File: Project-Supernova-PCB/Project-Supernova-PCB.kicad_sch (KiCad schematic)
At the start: 0 parts

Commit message: Add more parts of schematic
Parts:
- added C1, C2: 10u, Capacitor_SMD:C_1206_3216Metric_Pad1.33x1.80mm_HandSolder, symbol Device:C_Polarized
- added C103: 4.7u, Capacitor_SMD:C_1206_3216Metric_Pad1.33x1.80mm_HandSolder, symbol Device:C
- added C104, C105: NC, Capacitor_SMD:C_1206_3216Metric_Pad1.33x1.80mm_HandSolder, symbol Device:C
- added C106: 100n, Capacitor_SMD:C_1206_3216Metric_Pad1.33x1.80mm_HandSolder, symbol Device:C
- added J103, J106, J109: Screw_Terminal_01x02, TerminalBlock:TerminalBlock_bornier-2_P5.08mm, symbol Connector:Screw_Terminal_01x02
- added J104, J105: Conn_01x02, Connector_PinHeader_2.54mm:PinHeader_1x02_P2.54mm_Vertical, symbol Connector_Generic:Conn_01x02
- added J107: Conn_Coaxial, symbol Connector:Conn_Coaxial
- added J108: Conn_01x04, Connector_PinHeader_2.54mm:PinHeader_1x04_P2.54mm_Vertical, symbol Connector_Generic:Conn_01x04
- added J6, J7: 100k_Thermistor, Connector_PinHeader_2.54mm:PinHeader_1x02_P2.54mm_Vertical, symbol Connector_Generic:Conn_01x02
- added L101: 0, Inductor_SMD:L_1206_3216Metric_Pad1.42x1.75mm_HandSolder, symbol Device:L
- added Q101: Si1470DH, Package_TO_SOT_SMD:SOT-363_SC-70-6, symbol Transistor_FET:Si1442DH
- added R103: 10k, Resistor_SMD:R_1206_3216Metric_Pad1.30x1.75mm_HandSolder, symbol Device:R
- added R104, R2, R3: 4.7k, Resistor_SMD:R_1206_3216Metric_Pad1.30x1.75mm_HandSolder, symbol Device:R
- added SW101: SW_SPST, symbol Switch:SW_SPST
- added U101: BMP280-Module, Project-Supernova-Footprint-Lib:BMP280-Module, symbol Project-Supernova-Symbol-Lib:BMP280-Module
- added U102: GY-NEO6MV2-Module, Project-Supernova-Footprint-Lib:GY-NEO6MV2-Module, symbol Project-Supernova-Symbol-Lib:GY-NEO6MV2-Module
- added U103: LoRa-E5, Project-Supernova-Footprint-Lib:LoRa-E5, symbol Project-Supernova-Symbol-Lib:LoRa-E5
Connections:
- new net: C104.1, L101.1, U103.15 (RFIO)
- new net: J109.1 (Pin_1), Q101.1 (D), Q101.2 (D), Q101.5 (D), Q101.6 (D)
- new net: C105.1, J107.1 (In), L101.2
- new net: J103.2 (Pin_2), J104.2 (Pin_2), SW101.1 (A)
- new net +3V3: C103.1, C106.1, J105.2 (Pin_2), J106.2 (Pin_2), J108.1 (Pin_1), U101.1 (VCC), U102.1 (VCC), U103.1 (VCC)
- new net +BATT: J109.2 (Pin_2), R103.1, SW101.2 (B)
- new net BATT_SENSE: R103.2, R104.1
- new net DHT_DATA: J108.2 (Pin_2)
- new net GND: C1.2, C103.2, C104.2, C105.2, C106.2, C2.2, J103.1 (Pin_1), J104.1 (Pin_1), J105.1 (Pin_1), J106.1 (Pin_1), J107.2 (Ext), J108.4 (Pin_4), J6.1 (Pin_1), J7.1 (Pin_1), Q101.4 (S), R104.2, U101.2 (GND), U102.4 (GND), U103.14 (GND), U103.16 (GND), U103.2 (GND), U103.22 (GND)
- new net HEATER_EN: Q101.3 (G)
- new net LORA_UART_MISO: U103.10 (PB6)
- new net LORA_UART_MOSI: U103.9 (PB7)
- new net TEMP_SENSE_1: C1.1, J6.2 (Pin_2), R2.2
- new net TEMP_SENSE_2: C2.1, J7.2 (Pin_2), R3.2
- new net TEMP_V+: R2.1, R3.1
- no-connect marks 0 -> 3
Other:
- note added: "Board Heater"
- note added: "Divider Ratio: 4.7k/14.7k = 0.3197x 10V battery turns into 3.2V max"
- note added: "Looking at screen part, with pins pointing down, Pin 1 is on the left"
- note added: "Power Switch"
- note added: "Radio Section"
- note added: "TODO LM335"
- note added: "TODO add IMU, maybe"
- note added: "TODO add a "flight mode" switch which indicates when it's launched for debugging"
- note added: "TODO add microcontroller"
- note added: "To DHT22"
- note added: "To Heater"

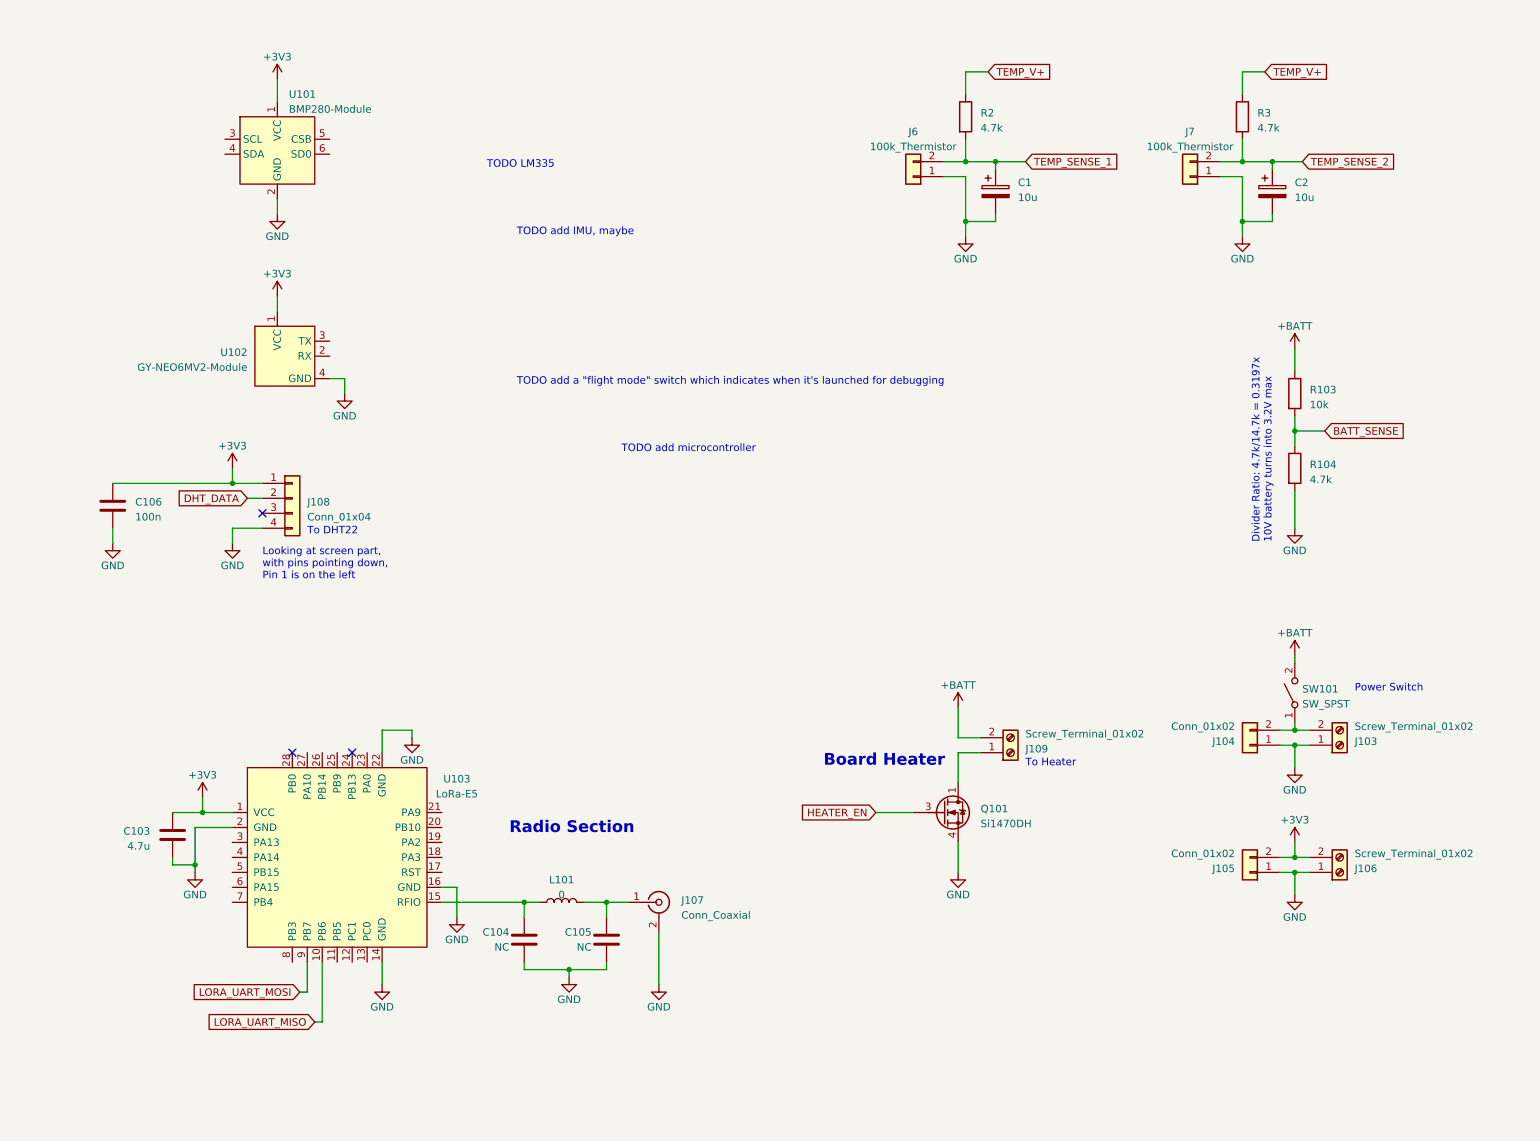
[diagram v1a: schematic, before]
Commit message: Update schematic docs, add TODO
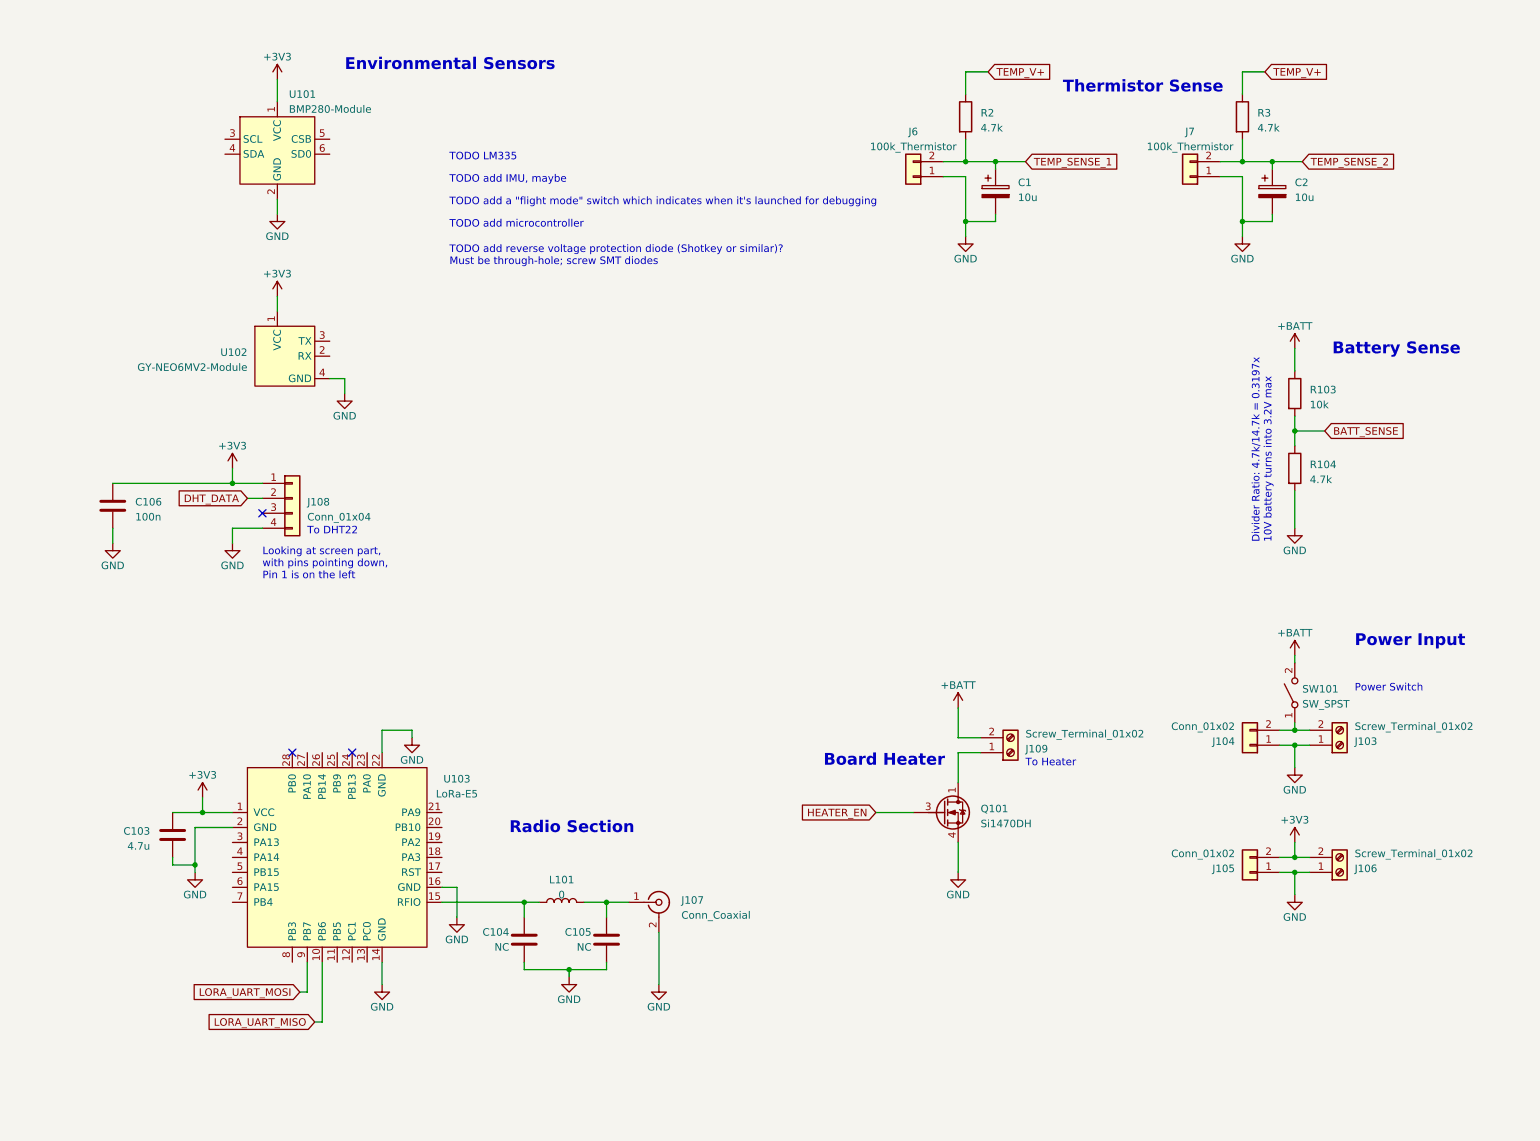
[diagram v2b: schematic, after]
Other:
- note added: "Battery Sense"
- note added: "Environmental Sensors"
- note added: "Power Input"
- note added: "TODO add reverse voltage protection diode (Shotkey or similar)? Must be through-hole; screw SMT diodes"
- note added: "Thermistor Sense"
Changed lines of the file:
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@@
   )
   (text "TODO add a \"flight mode\" switch which indicates when it's launched for debugging"
-    (at 99.06 77.47 0)
+    (at 87.63 46.99 0)
     (effects (font (size 1.27 1.27)) (justify left bottom))
   )
-  (text "TODO add microcontroller" (at 116.84 88.9 0)
+  (text "TODO add microcontroller" (at 87.63 50.8 0)
     (effects (font (size 1.27 1.27)) (justify left bottom))
   )
@@
     (at 55.88 110.49 0)
     (effects (font (size 1.27 1.27)) (justify left bottom))
+  )
+  (text "Power Input" (at 241.3 121.92 0)
+    (effects (font (size 2 2) (thickness 0.4) bold) (justify left bottom))
+  )
+  (text "TODO add reverse voltage protection diode (Shotkey or similar)?\nMust be through-hole; screw SMT diodes"
+    (at 87.63 57.15 0)
+    (effects (font (size 1.27 1.27)) (justify left bottom))
+  )
+  (text "Environmental Sensors" (at 69.85 24.13 0)
+    (effects (font (size 2 2) (thickness 0.4) bold) (justify left bottom))
   )
   (text "To Heater" (at 185.42 142.24 0)
@@
     (effects (font (size 1.27 1.27)) (justify left bottom))
   )
-  (text "TODO add IMU, maybe" (at 99.06 52.07 0)
+  (text "Thermistor Sense" (at 191.77 27.94 0)
+    (effects (font (size 2 2) (thickness 0.4) bold) (justify left bottom))
+  )
+  (text "TODO add IMU, maybe" (at 87.63 43.18 0)
     (effects (font (size 1.27 1.27)) (justify left bottom))
   )
-  (text "TODO LM335" (at 93.98 40.64 0)
+  (text "TODO LM335" (at 87.63 39.37 0)
     (effects (font (size 1.27 1.27)) (justify left bottom))
   )
+  (text "Battery Sense" (at 237.49 72.39 0)
+    (effects (font (size 2 2) (thickness 0.4) bold) (justify left bottom))
+  )
   (global_label "TEMP_V+" (shape input) (at 226.06 24.13 0) (fields_autoplaced)

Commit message: Add ESP32 microcontroller
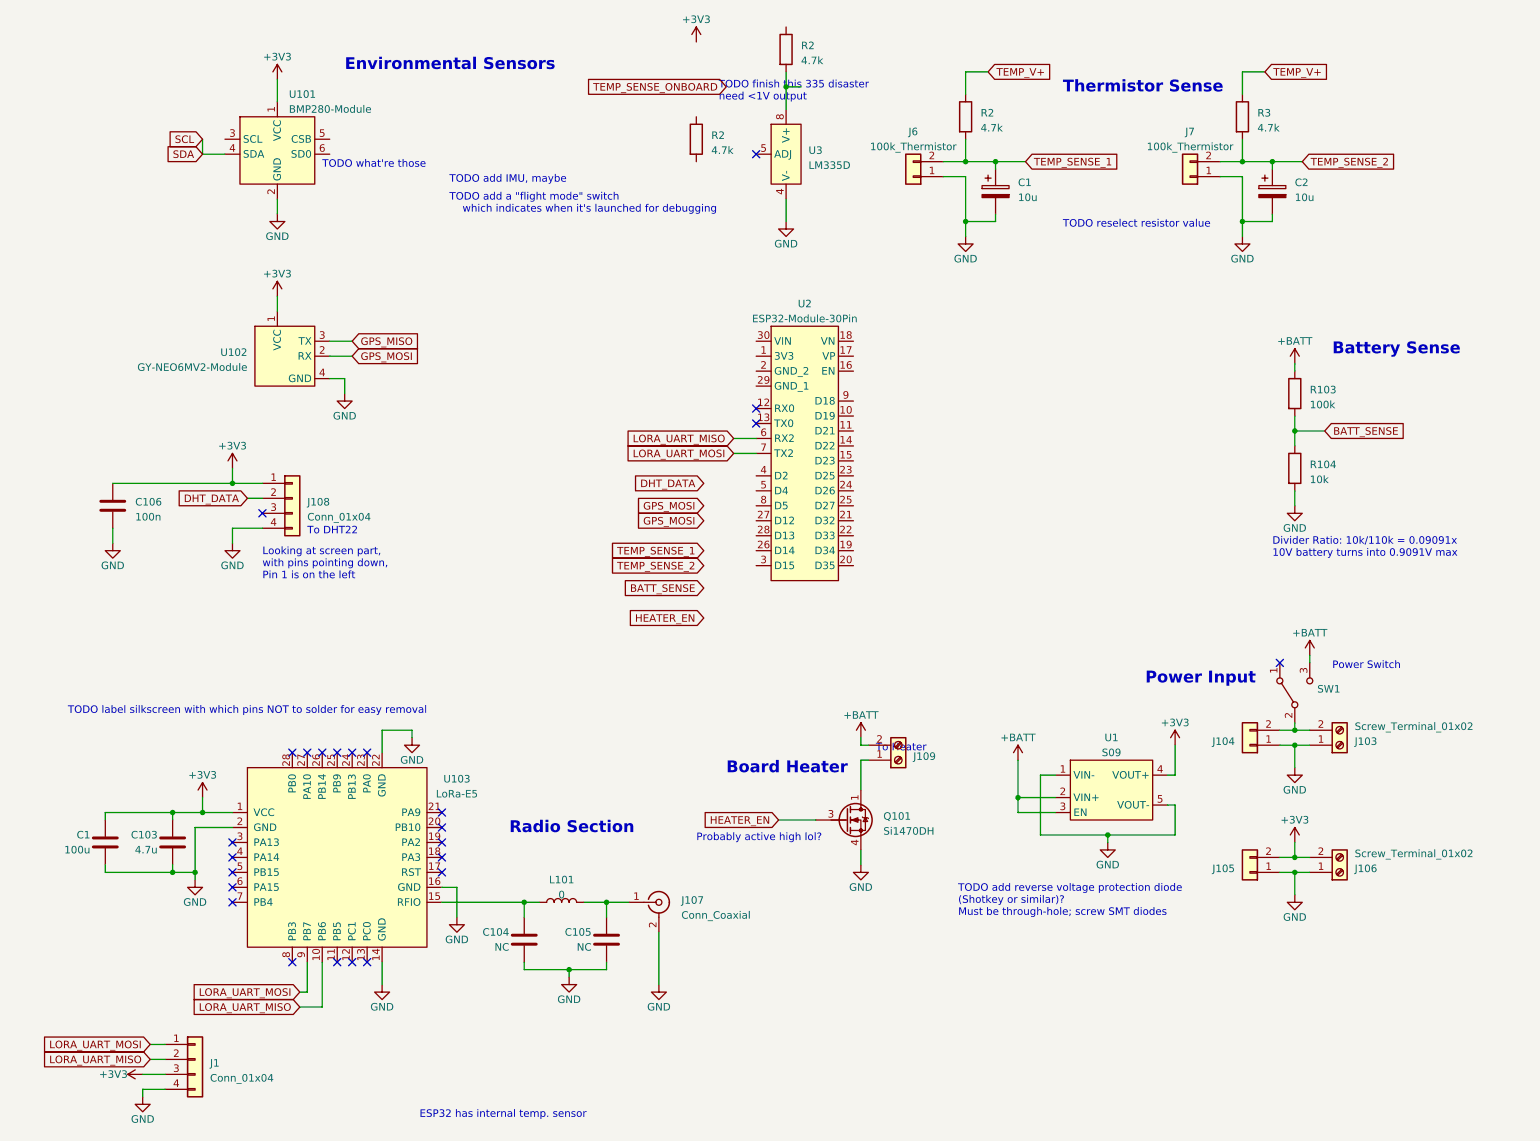
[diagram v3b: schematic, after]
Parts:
- removed SW101: SW_SPST, symbol Switch:SW_SPST
- added C1: 100u, Capacitor_SMD:C_1206_3216Metric_Pad1.33x1.80mm_HandSolder, symbol Device:C
- added J1: Conn_01x04, Connector_PinHeader_2.54mm:PinHeader_1x04_P2.54mm_Vertical, symbol Connector_Generic:Conn_01x04
- added R2 (x2): 4.7k, Resistor_SMD:R_1206_3216Metric_Pad1.30x1.75mm_HandSolder, symbol Device:R
- added SW1: SW_SPDT, Button_Switch_THT:SW_Slide_1P2T_CK_OS102011MS2Q, symbol Switch:SW_SPDT
- added U1: S09, Project-Supernova-Footprint-Lib:S09, symbol Project-Supernova-Symbol-Lib:S09_Buck_Boost
- added U2: ESP32-Module-30Pin, Project-Supernova-Footprint-Lib:ESP32-Module-30Pin, symbol Project-Supernova-Symbol-Lib:ESP32-Module
- added U3: LM335D, Package_SO:SOIC-8_3.9x4.9mm_P1.27mm, symbol Project-Supernova-Symbol-Lib:LM335D
- J107: footprint (none) -> Connector_Coaxial:SMA_Molex_73251-1153_EdgeMount_Horizontal
- R103: value 10k -> 100k
- R104: value 4.7k -> 10k
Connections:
- net +3V3: now also C1.1, J1.3 (Pin_3), U1.4 (VOUT+)
- net +BATT: now also SW1.3 (C), U1.2 (VIN+), U1.3 (EN)
- net GND: now also C1.2, J1.4 (Pin_4), U1.1 (VIN-), U1.5 (VOUT-), U3.4 (V-)
- net LORA_UART_MISO: now also J1.2 (Pin_2), U2.6 (RX2)
- net LORA_UART_MOSI: now also J1.1 (Pin_1), U2.7 (TX2)
- net at J103.2 (Pin_2), J104.2 (Pin_2): now also SW1.2 (B)
- net SCL: now reaches U101.4 (SDA)
- net GPS_MOSI: now reaches U102.2 (RX)
- net GPS_MISO: now reaches U102.3 (TX)
- new net: R2.2, U3.8 (V+)
- no-connect marks 3 -> 25
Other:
- note added: "Divider Ratio: 10k/110k = 0.09091x 10V battery turns into 0.9091V max"
- note added: "ESP32 has internal temp. sensor"
- note added: "Probably active high lol?"
- note added: "TODO finish this 335 disaster need <1V output"
- note added: "TODO label silkscreen with which pins NOT to solder for easy removal"
- note added: "TODO reselect resistor value"
- note added: "TODO what're those"
- note removed: "Divider Ratio: 4.7k/14.7k = 0.3197x 10V battery turns into 3.2V max"
- note removed: "TODO LM335"
- note removed: "TODO add microcontroller"
- moved on the sheet: C103, J109, Q101
